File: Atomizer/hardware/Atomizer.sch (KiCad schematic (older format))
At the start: 21 parts

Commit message: Added Atomizer Design and Code
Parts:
- R_PD1: footprint (none) -> Resistor_SMD:R_0805_2012Metric_Pad1.15x1.40mm_HandSolder
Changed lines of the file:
@@
 F 0 "R_PD1" H 4720 2445 50  0000 L CNN
 F 1 "22M" H 4720 2356 50  0000 L CNN
-F 2 "" V 4580 2400 50  0001 C CNN
+F 2 "Resistor_SMD:R_0805_2012Metric_Pad1.15x1.40mm_HandSolder" V 4580 2400 50  0001 C CNN
 F 3 "~" H 4650 2400 50  0001 C CNN
 	1    4650 2400

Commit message: Finished Atomizer RevB
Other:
- note added: "FOOTSWITCH"
- note added: "LFO"
- note removed: "3PDT"
- note removed: "CLOCK"
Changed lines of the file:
@@
 Text Label 4250 5750 0    50   ~ 0
 +5V_OPTO
-Text Notes 4850 3800 0    146  ~ 0
-3PDT
-Text Notes 7650 4550 0    146  ~ 0
-CLOCK
+Text Notes 4250 3800 0    146  ~ 0
+FOOTSWITCH
+Text Notes 7775 4575 0    146  ~ 0
+LFO
 Wire Notes Line
 	11500 10700 11500 7050

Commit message: Finished Atomizer RevB
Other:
- note added: "Guitar Fx pedals are \nCentre-Negative"
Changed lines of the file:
@@
 Text Label 4650 2850 1    50   ~ 0
 GND
+Text Notes 1450 9675 0    50   ~ 0
+Guitar Fx pedals are \nCentre-Negative
 $EndSCHEMATC

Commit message: Finished Atomizer RevA
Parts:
- J_IN1, J_OUT1: footprint custom_sockets:6_35MM_JACK_MONO_FlatTop -> custom_sockets:6_35MM_JACK_MONO_FlatTop_notab
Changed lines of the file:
@@
 F 0 "J_OUT1" H 13172 2355 50  0000 R CNN
 F 1 "JACK__MONO_2P_NC" H 13173 2400 50  0001 R CNN
-F 2 "custom_sockets:6_35MM_JACK_MONO_FlatTop" H 13650 2300 50  0001 C CNN
+F 2 "custom_sockets:6_35MM_JACK_MONO_FlatTop_notab" H 13650 2300 50  0001 C CNN
 F 3 "http://www.neutrik.us/en-us/plugs-jacks/slim-jacks/nrj4hf-1" H 13650 2300 50  0001 C CNN
 F 4 "550-10284G" H 13650 2300 50  0001 C CNN "MouserNo"
@@
 F 0 "J_IN1" H 2000 1900 50  0000 R CNN
 F 1 "JACK__MONO_2P_NC" H 1723 2200 50  0001 R CNN
-F 2 "custom_sockets:6_35MM_JACK_MONO_FlatTop" H 2200 2100 50  0001 C CNN
+F 2 "custom_sockets:6_35MM_JACK_MONO_FlatTop_notab" H 2200 2100 50  0001 C CNN
 F 3 "http://www.neutrik.us/en-us/plugs-jacks/slim-jacks/nrj4hf-1" H 2200 2100 50  0001 C CNN
 F 4 "550-10284G" H 2200 2100 50  0001 C CNN "MouserNo"

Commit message: Updated BOM. Converted to Mouser list. Moved LED away from switch
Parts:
- CP_INV1, CP_INV2: MouserNo (none) -> 140-VE100M1CTR0405
- C_BP3, C_BP4, C_BP5: MouserNo (none) -> 710-885012207098; Package/Case (none) -> 0805
- R1: MouserNo (none) -> 279-CRGP0805F1K0; Package/Case (none) -> 0805; Type (none) -> 1%
- R2: MouserNo (none) -> 71-CRCW0805330RFKEAC; Package/Case (none) -> 0805; Type (none) -> 1%
- R3: MouserNo (none) -> 279-CRGP0805F1K0; Package/Case (none) -> 0805
- R4: MouserNo (none) -> 667-ERJ-6ENF2700V; Package/Case (none) -> 0805; Type (none) -> 1%
- R5: MouserNo (none) -> 667-ERJ-6ENF47R0V; Package/Case (none) -> 0805
- R_GAIN1: MouserNo (none) -> 279-CRGCQ0805F2K7
- R_PD1: MouserNo (none) -> 755-UCR10EVHFSR022; Package/Case (none) -> 0805
- U_BUF1: Package/Case (none) -> SO-8
- U_INV1: Package/Case (none) -> SOIC-8
- U_NREG1, U_PREG1: Package/Case (none) -> SOT-223-4
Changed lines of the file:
@@
 F 6 "Microchip Technology" H 4200 8800 50  0001 C CNN "Mfr:"
 F 7 "Switching Voltage Regulators High Voltage" H 4200 8800 50  0001 C CNN "Type"
+F 8 "SOIC-8" H 4200 8800 50  0001 C CNN "Package/Case"
 	1    4200 8800
 	1    0    0    -1
@@
 F 2 "Capacitor_SMD:CP_Elec_4x5.4" H 5438 8700 50  0001 C CNN
 F 3 "~" H 5400 8850 50  0001 C CNN
+F 4 "140-VE100M1CTR0405" H 5400 8850 50  0001 C CNN "MouserNo"
 	1    5400 8850
 	-1   0    0    1
@@
 F 2 "Capacitor_SMD:CP_Elec_4x5.4" H 4838 8750 50  0001 C CNN
 F 3 "~" H 4800 8900 50  0001 C CNN
+F 4 "140-VE100M1CTR0405" H 4800 8900 50  0001 C CNN "MouserNo"
 	1    4800 8900
 	1    0    0    -1
@@
 F 6 "Texas Instruments" H 6750 8700 50  0001 C CNN "Mfr:"
 F 7 "Linear Voltage Regulators 3 Term Adj. Pos." H 6750 8700 50  0001 C CNN "Type"
+F 8 "SOT-223-4" H 6750 8700 50  0001 C CNN "Package/Case"
 	1    6750 8700
 	1    0    0    -1
@@
 F 2 "Resistor_SMD:R_0805_2012Metric_Pad1.15x1.40mm_HandSolder" V 7130 8900 50  0001 C CNN
 F 3 "~" H 7200 8900 50  0001 C CNN
+F 4 "71-CRCW0805330RFKEAC" H 7200 8900 50  0001 C CNN "MouserNo"
+F 5 "1%" H 7200 8900 50  0001 C CNN "Type"
+F 6 "0805" H 7200 8900 50  0001 C CNN "Package/Case"
 	1    7200 8900
 	1    0    0    -1
@@
 F 2 "Resistor_SMD:R_0805_2012Metric_Pad1.15x1.40mm_HandSolder" V 6680 9350 50  0001 C CNN
 F 3 "~" H 6750 9350 50  0001 C CNN
+F 4 "279-CRGP0805F1K0" H 6750 9350 50  0001 C CNN "MouserNo"
+F 5 "1%" H 6750 9350 50  0001 C CNN "Type"
+F 6 "0805" H 6750 9350 50  0001 C CNN "Package/Case"
 	1    6750 9350
 	1    0    0    -1
@@
 F 2 "Resistor_SMD:R_0805_2012Metric_Pad1.15x1.40mm_HandSolder" V 9030 8900 50  0001 C CNN
 F 3 "~" H 9100 8900 50  0001 C CNN
+F 4 "667-ERJ-6ENF2700V" H 9100 8900 50  0001 C CNN "MouserNo"
+F 5 "1%" H 9100 8900 50  0001 C CNN "Type"
+F 6 "0805" H 9100 8900 50  0001 C CNN "Package/Case"
 	1    9100 8900
 	-1   0    0    1
@@
 F 2 "Resistor_SMD:R_0805_2012Metric_Pad1.15x1.40mm_HandSolder" V 9030 9250 50  0001 C CNN
 F 3 "~" H 9100 9250 50  0001 C CNN
+F 4 "667-ERJ-6ENF47R0V" H 9100 9250 50  0001 C CNN "MouserNo"
+F 5 "0805" H 9100 9250 50  0001 C CNN "Package/Case"
 	1    9100 9250
 	1    0    0    -1
@@
 F 2 "Resistor_SMD:R_0805_2012Metric_Pad1.15x1.40mm_HandSolder" V 8530 9700 50  0001 C CNN
 F 3 "~" H 8600 9700 50  0001 C CNN
+F 4 "279-CRGP0805F1K0" H 8600 9700 50  0001 C CNN "MouserNo"
+F 5 "0805" H 8600 9700 50  0001 C CNN "Package/Case"
 	1    8600 9700
 	1    0    0    -1
@@
 F 6 "Diodes Incorporated" H 5700 2200 50  0001 C CNN "Mfr:"
 F 7 "JFET INPUT OP AMP LOW NOISE" H 5700 2200 50  0001 C CNN "Type"
+F 8 "SO-8" H 5700 2200 50  0001 C CNN "Package/Case"
 	1    5700 2200
 	1    0    0    -1
@@
 F 2 "Resistor_SMD:R_0805_2012Metric_Pad1.15x1.40mm_HandSolder" V 9580 3750 50  0001 C CNN
 F 3 "~" H 9650 3750 50  0001 C CNN
+F 4 "279-CRGCQ0805F2K7" H 9650 3750 50  0001 C CNN "MouserNo"
 	1    9650 3750
 	1    0    0    -1
@@
 F 6 "Diodes Incorporated" H 10150 2300 50  0001 C CNN "Mfr:"
 F 7 "JFET INPUT OP AMP LOW NOISE" H 10150 2300 50  0001 C CNN "Type"
+F 8 "SO-8" H 10150 2300 50  0001 C CNN "Package/Case"
 	2    10150 2300
 	1    0    0    -1
@@
 F 2 "Capacitor_SMD:C_0805_2012Metric_Pad1.15x1.40mm_HandSolder" H 10388 8550 50  0001 C CNN
 F 3 "~" H 10350 8700 50  0001 C CNN
+F 4 "710-885012207098" H 10350 8700 50  0001 C CNN "MouserNo"
+F 5 "0805" H 10350 8700 50  0001 C CNN "Package/Case"
 	1    10350 8700
 	1    0    0    1
@@
 F 2 "Capacitor_SMD:C_0805_2012Metric_Pad1.15x1.40mm_HandSolder" H 10388 8950 50  0001 C CNN
 F 3 "~" H 10350 9100 50  0001 C CNN
+F 4 "710-885012207098" H 10350 9100 50  0001 C CNN "MouserNo"
+F 5 "0805" H 10350 9100 50  0001 C CNN "Package/Case"
 	1    10350 9100
 	1    0    0    1
@@
 F 2 "Capacitor_SMD:C_0805_2012Metric_Pad1.15x1.40mm_HandSolder" H 3338 9000 50  0001 C CNN
 F 3 "~" H 3300 9150 50  0001 C CNN
+F 4 "710-885012207098" H 3300 9150 50  0001 C CNN "MouserNo"
+F 5 "0805" H 3300 9150 50  0001 C CNN "Package/Case"
 	1    3300 9150
 	1    0    0    1
@@
 F 6 "Texas Instruments" H 8600 8700 50  0001 C CNN "Mfr:"
 F 7 "Linear Voltage Regulators 3-TERMINAL ADJ NEG REG" H 8600 8700 50  0001 C CNN "Type"
+F 8 "SOT-223-4" H 8600 8700 50  0001 C CNN "Package/Case"
 	1    8600 8700
 	1    0    0    1
@@
 F 2 "Resistor_SMD:R_0805_2012Metric_Pad1.15x1.40mm_HandSolder" V 4580 2400 50  0001 C CNN
 F 3 "~" H 4650 2400 50  0001 C CNN
+F 4 "755-UCR10EVHFSR022" H 4650 2400 50  0001 C CNN "MouserNo"
+F 5 "0805" H 4650 2400 50  0001 C CNN "Package/Case"
 	1    4650 2400
 	1    0    0    -1

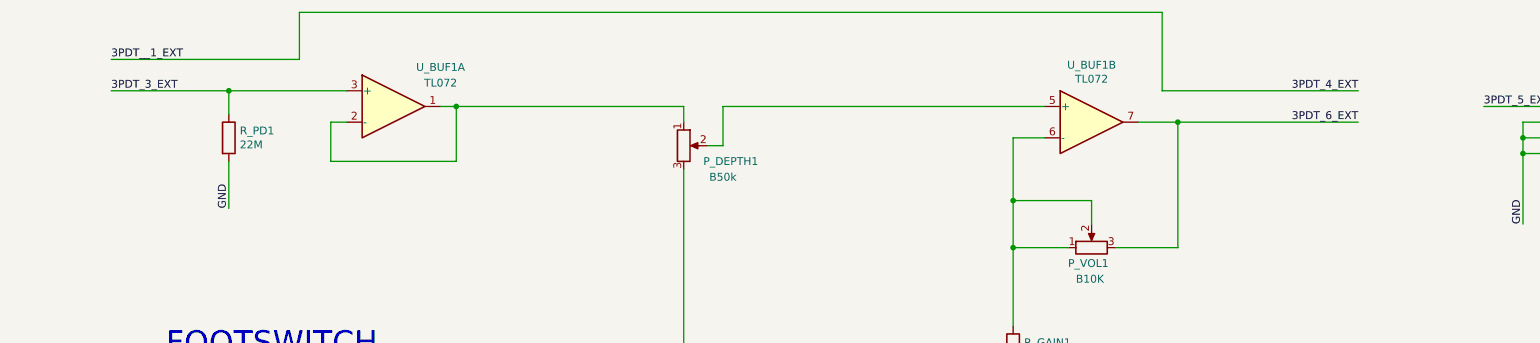
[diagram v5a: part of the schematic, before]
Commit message: updated atomizer
- changed input pulldown resistor from 22M to 1M
- added output lpf filter (1uF, 100K)
- updated docs
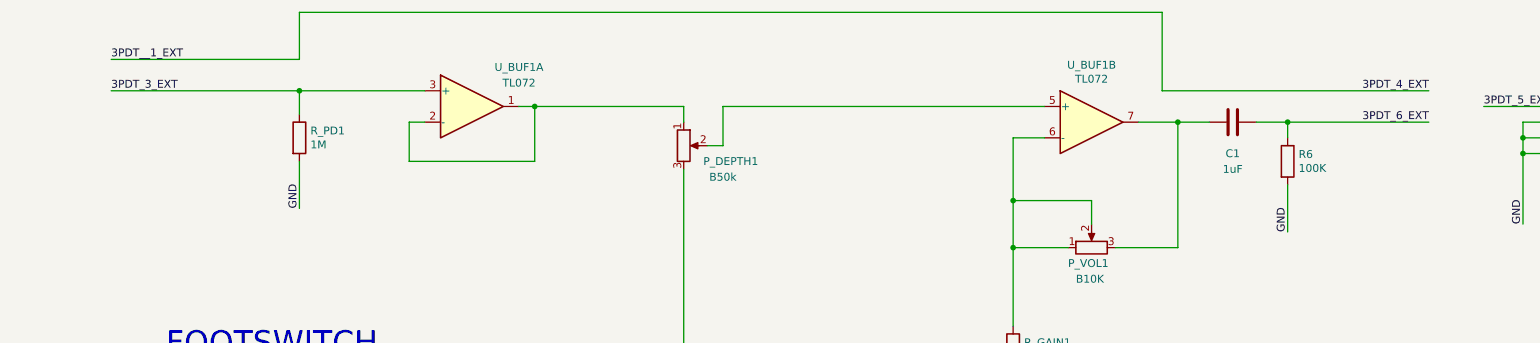
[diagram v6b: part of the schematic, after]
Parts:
- added C1: 1uF, Capacitor_SMD:C_0805_2012Metric_Pad1.15x1.40mm_HandSolder, symbol Device:C
- added R6: 100K, Resistor_SMD:R_0805_2012Metric_Pad1.15x1.40mm_HandSolder, symbol Device:R
- R_PD1: value 22M -> 1M
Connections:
- wire segments 118 -> 122
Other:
- moved on the sheet: R_PD1, U_BUF1A
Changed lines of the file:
@@
 encoding utf-8
 Sheet 1 3
-Title ""
-Date ""
-Rev ""
+Title "Atomizer FX pedal"
+Date "2019-06-01"
+Rev "B"
 Comp ""
-Comment1 ""
-Comment2 ""
+Comment1 "Design by Chris Sutton"
+Comment2 "Optical Tremolo with digital timer"
 Comment3 ""
 Comment4 ""
@@
 L Amplifier_Operational:TL072 U_BUF1
 U 1 1 5BE1E27D
-P 5700 2200
-F 0 "U_BUF1" H 6000 2450 50  0000 C CNN
-F 1 "TL072" H 6000 2350 50  0000 C CNN
-F 2 "Package_SO:SOIC-8_3.9x4.9mm_P1.27mm" H 5700 2200 50  0001 C CNN
-F 3 "http://www.ti.com/lit/ds/symlink/tl071.pdf" H 5700 2200 50  0001 C CNN
-F 4 "621-TL072SG-13" H 5700 2200 50  0001 C CNN "MouserNo"
-F 5 "TL072SG-13" H 5700 2200 50  0001 C CNN "Mfr. No:"
-F 6 "Diodes Incorporated" H 5700 2200 50  0001 C CNN "Mfr:"
-F 7 "JFET INPUT OP AMP LOW NOISE" H 5700 2200 50  0001 C CNN "Type"
-F 8 "SO-8" H 5700 2200 50  0001 C CNN "Package/Case"
-	1    5700 2200
+P 6200 2200
+F 0 "U_BUF1" H 6500 2450 50  0000 C CNN
+F 1 "TL072" H 6500 2350 50  0000 C CNN
+F 2 "Package_SO:SOIC-8_3.9x4.9mm_P1.27mm" H 6200 2200 50  0001 C CNN
+F 3 "http://www.ti.com/lit/ds/symlink/tl071.pdf" H 6200 2200 50  0001 C CNN
+F 4 "621-TL072SG-13" H 6200 2200 50  0001 C CNN "MouserNo"
+F 5 "TL072SG-13" H 6200 2200 50  0001 C CNN "Mfr. No:"
+F 6 "Diodes Incorporated" H 6200 2200 50  0001 C CNN "Mfr:"
+F 7 "JFET INPUT OP AMP LOW NOISE" H 6200 2200 50  0001 C CNN "Type"
+F 8 "SO-8" H 6200 2200 50  0001 C CNN "Package/Case"
+	1    6200 2200
 	1    0    0    -1
 $EndComp
@@
 $EndComp
 Wire Wire Line
-	6000 2200 6100 2200
-Wire Wire Line
-	5400 2300 5300 2300
-Wire Wire Line
-	5300 2300 5300 2550
-Wire Wire Line
-	5300 2550 6100 2550
-Wire Wire Line
-	6100 2550 6100 2200
+	6500 2200 6600 2200
+Wire Wire Line
+	5900 2300 5800 2300
+Wire Wire Line
+	5800 2300 5800 2550
+Wire Wire Line
+	5800 2550 6600 2550
+Wire Wire Line
+	6600 2550 6600 2200
 $Comp
 L Connector:Jack-DC J_PWR1
@@
 	3300 9300 3300 9950
 Wire Wire Line
-	7550 2200 6100 2200
-Connection ~ 6100 2200
+	7550 2200 6600 2200
+Connection ~ 6600 2200
 $Comp
 L Regulator_Linear:LM337_SOT223 U_NREG1
@@
 	13200 2200 12650 2200
 Wire Wire Line
-	11850 2300 10700 2300
-Connection ~ 10700 2300
-Wire Wire Line
-	11850 2100 10600 2100
+	12300 2100 10600 2100
 Wire Wire Line
 	10600 2100 10600 1600
 Wire Wire Line
 	3100 2000 2650 2000
-Wire Wire Line
-	3900 2100 4650 2100
 Wire Wire Line
 	3900 1900 5100 1900
@@
 Text Label 12650 2200 0    50   ~ 0
 3PDT_5_EXT
-Text Label 11850 2100 2    50   ~ 0
+Text Label 12300 2100 2    50   ~ 0
 3PDT_4_EXT
-Text Label 11850 2300 2    50   ~ 0
+Text Label 12300 2300 2    50   ~ 0
 3PDT_6_EXT
 Text Label 4250 4750 0    50   ~ 0
@@
 L Device:R R_PD1
 U 1 1 5BFF515B
-P 4650 2400
-F 0 "R_PD1" H 4720 2445 50  0000 L CNN
-F 1 "22M" H 4720 2356 50  0000 L CNN
-F 2 "Resistor_SMD:R_0805_2012Metric_Pad1.15x1.40mm_HandSolder" V 4580 2400 50  0001 C CNN
-F 3 "~" H 4650 2400 50  0001 C CNN
-F 4 "755-UCR10EVHFSR022" H 4650 2400 50  0001 C CNN "MouserNo"
-F 5 "0805" H 4650 2400 50  0001 C CNN "Package/Case"
-	1    4650 2400
-	1    0    0    -1
-$EndComp
-Wire Wire Line
-	4650 2250 4650 2100
-Connection ~ 4650 2100
-Wire Wire Line
-	4650 2100 5400 2100
-Wire Wire Line
-	4650 2550 4650 2850
-Text Label 4650 2850 1    50   ~ 0
+P 5100 2400
+F 0 "R_PD1" H 5170 2445 50  0000 L CNN
+F 1 "1M" H 5170 2356 50  0000 L CNN
+F 2 "Resistor_SMD:R_0805_2012Metric_Pad1.15x1.40mm_HandSolder" V 5030 2400 50  0001 C CNN
+F 3 "~" H 5100 2400 50  0001 C CNN
+F 4 "755-UCR10EVHFSR022" H 5100 2400 50  0001 C CNN "MouserNo"
+F 5 "0805" H 5100 2400 50  0001 C CNN "Package/Case"
+	1    5100 2400
+	1    0    0    -1
+$EndComp
+Wire Wire Line
+	5100 2250 5100 2100
+Wire Wire Line
+	5100 2550 5100 2850
+Text Label 5100 2850 1    50   ~ 0
 GND
 Text Notes 1450 9675 0    50   ~ 0
 Guitar Fx pedals are \nCentre-Negative
+$Comp
+L Device:C C1
+U 1 1 5CF35DED
+P 11050 2300
+F 0 "C1" V 10850 2300 50  0000 C CNN
+F 1 "1uF" V 10750 2300 50  0000 C CNN
+F 2 "Capacitor_SMD:C_0805_2012Metric_Pad1.15x1.40mm_HandSolder" H 11088 2150 50  0001 C CNN
+F 3 "~" H 11050 2300 50  0001 C CNN
+	1    11050 2300
+	0    1    -1   0
+$EndComp
+Connection ~ 5100 2100
+Wire Wire Line
+	5100 2100 5900 2100
+Wire Wire Line
+	3900 2100 5100 2100
+$Comp
+L Device:R R6
+U 1 1 5CF5D952
+P 11400 2550
+F 0 "R6" H 11470 2595 50  0000 L CNN
+F 1 "100K" H 11470 2506 50  0000 L CNN
+F 2 "Resistor_SMD:R_0805_2012Metric_Pad1.15x1.40mm_HandSolder" V 11330 2550 50  0001 C CNN
+F 3 "~" H 11400 2550 50  0001 C CNN
+	1    11400 2550
+	1    0    0    -1
+$EndComp
+Wire Wire Line
+	11400 2400 11400 2300
+Wire Wire Line
+	11400 2300 11200 2300
+Wire Wire Line
+	10900 2300 10700 2300
+Connection ~ 10700 2300
+Wire Wire Line
+	11400 2300 12300 2300
+Connection ~ 11400 2300
+Wire Wire Line
+	11400 2700 11400 3000
+Text Label 11400 3000 1    50   ~ 0
+GND
 $EndSCHEMATC

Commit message: updates
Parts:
- U_INV1: symbol Converter_DCDC:TC7662Bx0A -> Atomizer-rescue:TC7662Bx0A-Converter_DCDC
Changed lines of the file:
@@
 EESchema Schematic File Version 4
 LIBS:Atomizer-cache
-EELAYER 26 0
+EELAYER 29 0
 EELAYER END
 $Descr A3 16535 11693
@@
 $EndDescr
 $Comp
-L Converter_DCDC:TC7662Bx0A U_INV1
+L Atomizer-rescue:TC7662Bx0A-Converter_DCDC U_INV1
 U 1 1 5BE0D4DB
 P 4200 8800
